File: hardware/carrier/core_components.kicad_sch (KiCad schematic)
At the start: 52 parts, among them J1 PANEL, J2 CARDKB, J3 HAPTIC, J4 EXT_LED, J5 PIEZ, J8 FRONTLIGHT, M1 Walter, Q1 UMH3N, Q2 SI1308EDL, Q3 MMST3904, SW1 KMR221GLFS, U1 CP2102N-A02-GQFN24, U2 SN74LVC2G126DCUR, U3 DRV2605LDGSR, U4 LIS2DW12TR

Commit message: Carrier: close the outline, tidy silkscreen, add GND pours (DRC 278 -> 28)
- Edge.Cuts rebuilt as a single closed loop (right edge 113.15, SIM notch, 1 mm corners)
- 0402/LGA parts moved to pager-carrier:*_NoSilk footprints (library copies without the
  silk outline), schematic fields updated; J6 silk box stops short of the shield pads;
  reference text re-placed or hidden; stale board texts removed
- GND pours both layers (0.2 clearance, thermal reliefs), 3 stitching vias for the
  top-side GND groups that had no path to the plane; all GND connected
- Remaining: 4 owner routing clearances, H1-H3 parked off-board, 2 unrouted nets

Co-Authored-By: Claude Fable 5.1 <noreply@anthropic.com>
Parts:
- C10, C11, C12, C2, C3, C4, C5, C9: footprint Capacitor_SMD:C_0402_1005Metric -> pager-carrier:C_0402_1005Metric_NoSilk
- R1, R10, R11, R14, R15, R16, R17, R18, R19, R2, R20, R21, R22, R3, R39, R4, R5, R6, R7, R8, R9: footprint Resistor_SMD:R_0402_1005Metric -> pager-carrier:R_0402_1005Metric_NoSilk
- U4: footprint Package_LGA:LGA-12_2x2mm_P0.5mm -> pager-carrier:LGA-12_2x2mm_P0.5mm_NoSilk
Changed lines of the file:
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@@
 			)
 		)
-		(property "Footprint" "Resistor_SMD:R_0402_1005Metric"
+		(property "Footprint" "pager-carrier:R_0402_1005Metric_NoSilk"
 			(at 196.85 39.37 0)
 			(hide yes)
@@
 			)
 		)
-		(property "Footprint" "Resistor_SMD:R_0402_1005Metric"
+		(property "Footprint" "pager-carrier:R_0402_1005Metric_NoSilk"
 			(at 199.39 101.6 0)
 			(hide yes)
@@
 			)
 		)
-		(property "Footprint" "Capacitor_SMD:C_0402_1005Metric"
+		(property "Footprint" "pager-carrier:C_0402_1005Metric_NoSilk"
 			(at 222.25 217.17 0)
 			(hide yes)
@@
 			)
 		)
-		(property "Footprint" "Resistor_SMD:R_0402_1005Metric"
+		(property "Footprint" "pager-carrier:R_0402_1005Metric_NoSilk"
 			(at 44.45 196.85 0)
 			(hide yes)
@@
 			)
 		)
-		(property "Footprint" "Resistor_SMD:R_0402_1005Metric"
+		(property "Footprint" "pager-carrier:R_0402_1005Metric_NoSilk"
 			(at 274.32 173.99 0)
 			(hide yes)
@@
 			)
 		)
-		(property "Footprint" "Package_LGA:LGA-12_2x2mm_P0.5mm"
+		(property "Footprint" "pager-carrier:LGA-12_2x2mm_P0.5mm_NoSilk"
 			(at 387.35 63.5 0)
 			(hide yes)
@@
 			)
 		)
-		(property "Footprint" "Resistor_SMD:R_0402_1005Metric"
+		(property "Footprint" "pager-carrier:R_0402_1005Metric_NoSilk"
 			(at 288.29 48.26 0)
 			(hide yes)
@@
 			)
 		)
-		(property "Footprint" "Resistor_SMD:R_0402_1005Metric"
+		(property "Footprint" "pager-carrier:R_0402_1005Metric_NoSilk"
 			(at 384.81 173.99 0)
 			(hide yes)
@@
 			)
 		)
-		(property "Footprint" "Capacitor_SMD:C_0402_1005Metric"
+		(property "Footprint" "pager-carrier:C_0402_1005Metric_NoSilk"
 			(at 318.77 176.53 0)
 			(hide yes)
@@
 			)
 		)
-		(property "Footprint" "Capacitor_SMD:C_0402_1005Metric"
+		(property "Footprint" "pager-carrier:C_0402_1005Metric_NoSilk"
 			(at 110.49 110.49 0)
 			(hide yes)
@@
 			)
 		)
-		(property "Footprint" "Resistor_SMD:R_0402_1005Metric"
+		(property "Footprint" "pager-carrier:R_0402_1005Metric_NoSilk"
 			(at 186.69 247.65 0)
 			(hide yes)
@@
 			)
 		)
-		(property "Footprint" "Resistor_SMD:R_0402_1005Metric"
+		(property "Footprint" "pager-carrier:R_0402_1005Metric_NoSilk"
 			(at 345.44 40.64 0)
 			(hide yes)
@@
 			)
 		)
-		(property "Footprint" "Resistor_SMD:R_0402_1005Metric"
+		(property "Footprint" "pager-carrier:R_0402_1005Metric_NoSilk"
 			(at 387.35 147.32 0)
 			(hide yes)
@@
 			)
 		)
-		(property "Footprint" "Capacitor_SMD:C_0402_1005Metric"
+		(property "Footprint" "pager-carrier:C_0402_1005Metric_NoSilk"
 			(at 33.02 233.68 0)
 			(hide yes)
@@
 			)
 		)
-		(property "Footprint" "Capacitor_SMD:C_0402_1005Metric"
+		(property "Footprint" "pager-carrier:C_0402_1005Metric_NoSilk"
 			(at 304.8 168.91 0)
 			(hide yes)
@@
 			)
 		)
-		(property "Footprint" "Resistor_SMD:R_0402_1005Metric"
+		(property "Footprint" "pager-carrier:R_0402_1005Metric_NoSilk"
 			(at 384.81 191.77 0)
 			(hide yes)
@@
 			)
 		)
-		(property "Footprint" "Resistor_SMD:R_0402_1005Metric"
+		(property "Footprint" "pager-carrier:R_0402_1005Metric_NoSilk"
 			(at 170.18 218.44 0)
 			(hide yes)
@@
 			)
 		)
-		(property "Footprint" "Resistor_SMD:R_0402_1005Metric"
+		(property "Footprint" "pager-carrier:R_0402_1005Metric_NoSilk"
 			(at 44.45 212.09 0)
 			(hide yes)
@@
 			)
 		)
-		(property "Footprint" "Resistor_SMD:R_0402_1005Metric"
+		(property "Footprint" "pager-carrier:R_0402_1005Metric_NoSilk"
 			(at 199.39 113.03 0)
 			(hide yes)
@@
 			)
 		)
-		(property "Footprint" "Resistor_SMD:R_0402_1005Metric"
+		(property "Footprint" "pager-carrier:R_0402_1005Metric_NoSilk"
 			(at 402.59 180.34 0)
 			(hide yes)
@@
 			)
 		)
-		(property "Footprint" "Resistor_SMD:R_0402_1005Metric"
+		(property "Footprint" "pager-carrier:R_0402_1005Metric_NoSilk"
 			(at 345.44 44.45 0)
 			(hide yes)
@@
 			)
 		)
-		(property "Footprint" "Resistor_SMD:R_0402_1005Metric"
+		(property "Footprint" "pager-carrier:R_0402_1005Metric_NoSilk"
 			(at 123.19 100.33 0)
 			(hide yes)
@@
 			)
 		)
-		(property "Footprint" "Capacitor_SMD:C_0402_1005Metric"
+		(property "Footprint" "pager-carrier:C_0402_1005Metric_NoSilk"
 			(at 101.6 213.36 0)
 			(hide yes)
@@
 			)
 		)
-		(property "Footprint" "Capacitor_SMD:C_0402_1005Metric"
+		(property "Footprint" "pager-carrier:C_0402_1005Metric_NoSilk"
 			(at 109.22 213.36 0)
 			(hide yes)
@@
 			)
 		)
-		(property "Footprint" "Resistor_SMD:R_0402_1005Metric"
+		(property "Footprint" "pager-carrier:R_0402_1005Metric_NoSilk"
 			(at 124.46 229.87 0)
 			(hide yes)
@@
 			)
 		)
-		(property "Footprint" "Resistor_SMD:R_0402_1005Metric"
+		(property "Footprint" "pager-carrier:R_0402_1005Metric_NoSilk"
 			(at 54.61 189.23 0)
 			(hide yes)
@@
 			)
 		)
-		(property "Footprint" "Resistor_SMD:R_0402_1005Metric"
+		(property "Footprint" "pager-carrier:R_0402_1005Metric_NoSilk"
 			(at 288.29 53.34 0)
 			(hide yes)
@@
 			)
 		)
-		(property "Footprint" "Resistor_SMD:R_0402_1005Metric"
+		(property "Footprint" "pager-carrier:R_0402_1005Metric_NoSilk"
 			(at 120.65 229.87 0)
 			(hide yes)
@@
 			)
 		)
-		(property "Footprint" "Resistor_SMD:R_0402_1005Metric"
+		(property "Footprint" "pager-carrier:R_0402_1005Metric_NoSilk"
 			(at 148.59 218.44 0)
 			(hide yes)
@@
 			)
 		)
-		(property "Footprint" "Capacitor_SMD:C_0402_1005Metric"
+		(property "Footprint" "pager-carrier:C_0402_1005Metric_NoSilk"
 			(at 334.01 66.04 0)
 			(hide yes)

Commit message: BOM: move six passives to JLC basic parts, fix connector LCSC codes (no footprint changes)
Carrier: R32 2.2M -> 1M (C26083), C14 22nF -> 100nF (C1525), R1 22.1k -> 22k (C25768),
R2 47.5k -> 47k (C25792); J1 LCSC C160407 (SM08B), J2 MPN/LCSC SM04B-SRSS-TB C160404
to match its SH footprint.
Panel: C11 4.7uF under basic code C19666, D1-D3 NSR0530 -> B5819W (C8598, SOD-123 as
already on the board), R4 2.2R gets C22939.
Board footprint fields updated to match. ERC clean on both.

Co-Authored-By: Claude Fable 5.1 <noreply@anthropic.com>
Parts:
- J1: LCSC C160409 -> C160407; MPN SM8B-SRSS-TB -> SM08B-SRSS-TB
- J2: LCSC C265102 -> C160404; MPN S4B-PH-SM4-TB -> SM04B-SRSS-TB
- R1: value 22.1k -> 22k; LCSC C43473 -> C25768; MPN 0402WGF2212TCE -> 0402WGF2202TCE
- R2: value 47.5k -> 47k; LCSC C25896 -> C25792; MPN 0402WGF4752TCE -> 0402WGF4702TCE
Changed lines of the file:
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@@
 			)
 		)
-		(property "MPN" "SM8B-SRSS-TB"
+		(property "MPN" "SM08B-SRSS-TB"
 			(at 181.61 69.85 0)
 			(hide yes)
@@
 			)
 		)
-		(property "LCSC" "C160409"
+		(property "LCSC" "C160407"
 			(at 181.61 72.39 0)
 			(hide yes)
@@
 			)
 		)
-		(property "Value" "22.1k"
+		(property "Value" "22k"
 			(at 36.322 196.85 0)
 			(show_name no)
@@
 			)
 		)
-		(property "MPN" "0402WGF2212TCE"
+		(property "MPN" "0402WGF2202TCE"
 			(at 43.18 210.82 0)
 			(hide yes)
@@
 			)
 		)
-		(property "LCSC" "C43473"
+		(property "LCSC" "C25768"
 			(at 43.18 213.36 0)
 			(hide yes)
@@
 			)
 		)
-		(property "MPN" "S4B-PH-SM4-TB"
+		(property "MPN" "SM04B-SRSS-TB"
 			(at 266.7 48.26 0)
 			(hide yes)
@@
 			)
 		)
-		(property "LCSC" "C265102"
+		(property "LCSC" "C160404"
 			(at 266.7 45.72 0)
 			(hide yes)
@@
 			)
 		)
-		(property "Value" "47.5k"
+		(property "Value" "47k"
 			(at 35.56 212.344 0)
 			(show_name no)
@@
 			)
 		)
-		(property "MPN" "0402WGF4752TCE"
+		(property "MPN" "0402WGF4702TCE"
 			(at 43.18 226.06 0)
 			(hide yes)
@@
 			)
 		)
-		(property "LCSC" "C25896"
+		(property "LCSC" "C25792"
 			(at 43.18 228.6 0)
 			(hide yes)

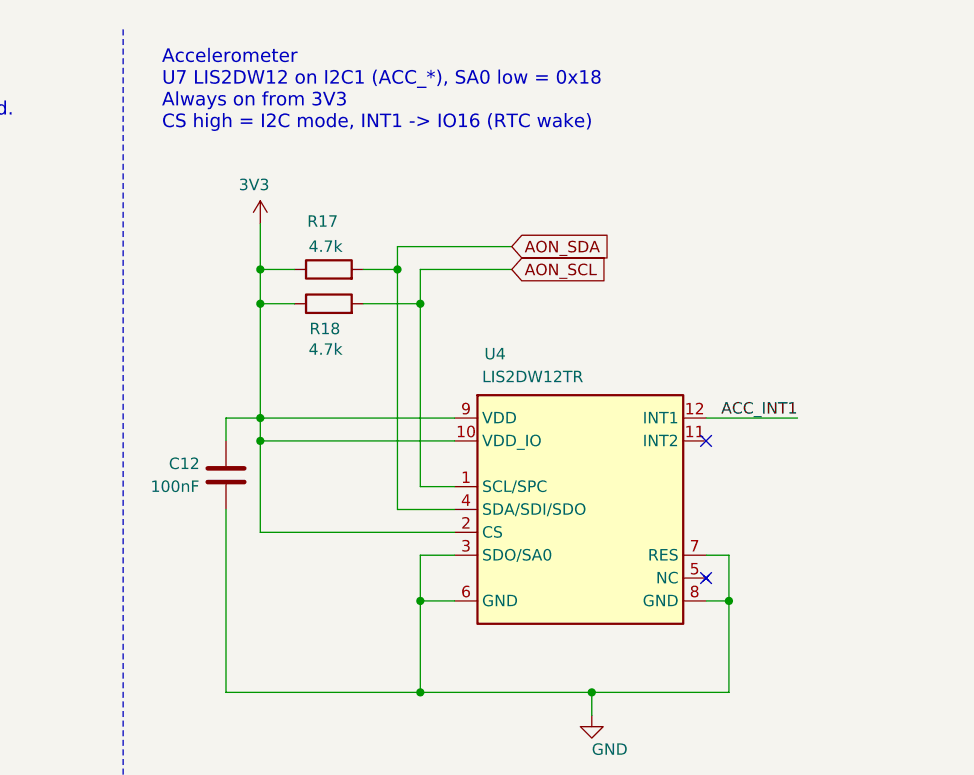
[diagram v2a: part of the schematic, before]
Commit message: Carrier: accelerometer -> MSKSEMI LIS2DW12TR-MS for Economic PCBA, JLC production files
U4 ST LIS2DW12TR (C189624, JLC "Standard Only") -> MSKSEMI LIS2DW12TR-MS
(C50385411, Economic and Standard). Same LGA-12 2x2 land pattern and pin-1
corner, different pinout (new project symbol); owner rerouted U4. The part is
an SC7A20-class die: WHO_AM_I 0x11, LIS3DH-style registers, I2C 0x18 with
SDO/SA0 low. Firmware follow-ups: accept 0x11, set SDO_PU in reg 0x57.

Also adds the ShouHan J6/SW2 footprints from the stock-part swap, the
Fabrication Toolkit options and production outputs (carrier and panel), and
the panel STEP. DRC 0 errors / 0 unconnected; ERC unchanged vs HEAD.

Co-Authored-By: Claude Opus 5.5 <noreply@anthropic.com>
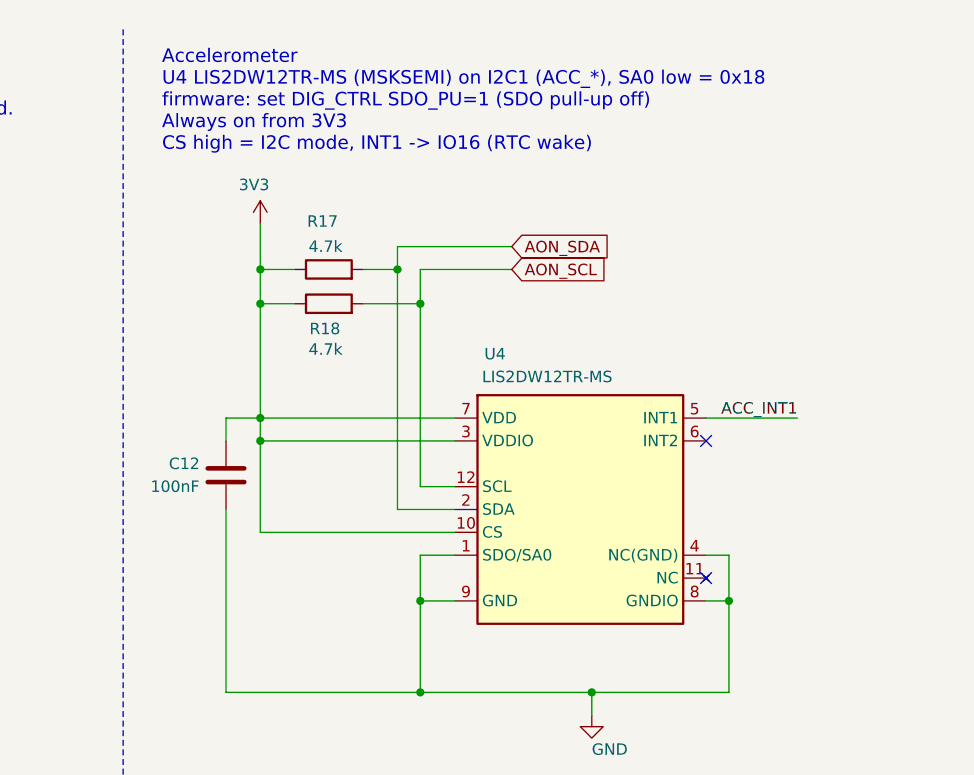
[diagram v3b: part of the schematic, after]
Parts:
- U4: value LIS2DW12TR -> LIS2DW12TR-MS; symbol pager-carrier:LIS2DW12TR -> pager-carrier:LIS2DW12TR-MS; LCSC C189624 -> C50385411; MPN LIS2DW12TR -> LIS2DW12TR-MS; Note (none) -> MSKSEMI SC7A20-class part, WHO_AM_I 0x11, LIS3DH-style regi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
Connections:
- net 3V3: now also U4.3 (VDDIO), U4.7 (VDD); no longer U4.2 (CS), U4.9 (VDD)
- net ACC_INT1: now also U4.5 (INT1); no longer U4.12 (INT1)
- net AON_SCL: now also U4.12 (SCL); no longer U4.1 (SCL/SPC)
- net AON_SDA: now also U4.2 (SDA); no longer U4.4 (SDA/SDI/SDO)
- net GND: now also U4.1 (SDO/SA0), U4.4 (NC(GND)), U4.9 (GND); no longer U4.3 (SDO/SA0), U4.6 (GND), U4.7 (RES)
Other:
- note added: "Accelerometer U4 LIS2DW12TR-MS (MSKSEMI) on I2C1 (ACC_*), SA0 low = 0x18 firmware: set DIG_CTRL SDO_PU=1 (SDO pull-up off) Always on from 3V3 CS high = I2C mode, INT1 -> IO16 (RTC wake)"
- note removed: "Accelerometer U7 LIS2DW12 on I2C1 (ACC_*), SA0 low = 0x18 Always on from 3V3 CS high = I2C mode, INT1 -> IO16 (RTC wake)"
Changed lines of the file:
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@@
 		)
 	)
-	(text "Accelerometer\nU7 LIS2DW12 on I2C1 (ACC_*), SA0 low = 0x18\nAlways on from 3V3\nCS high = I2C mode, INT1 -> IO16 (RTC wake)"
+	(text "Accelerometer\nU4 LIS2DW12TR-MS (MSKSEMI) on I2C1 (ACC_*), SA0 low = 0x18\nfirmware: set DIG_CTRL SDO_PU=1 (SDO pull-up off)\nAlways on from 3V3\nCS high = I2C mode, INT1 -> IO16 (RTC wake)"
 		(exclude_from_sim no)
 		(at 325.628 17.526 0)
@@
 	)
 	(symbol
-		(lib_id "pager-carrier:LIS2DW12TR")
+		(lib_id "pager-carrier:LIS2DW12TR-MS")
 		(at 372.11 68.58 0)
 		(unit 1)
@@
 			)
 		)
-		(property "Value" "LIS2DW12TR"
+		(property "Value" "LIS2DW12TR-MS"
 			(at 361.188 53.848 0)
 			(show_name no)
@@
 			)
 		)
-		(property "Datasheet" "https://www.st.com/resource/en/datasheet/lis2dw12.pdf"
+		(property "Datasheet" "https://www.lcsc.com/datasheet/C50385411.pdf"
 			(at 387.35 66.04 0)
 			(hide yes)
@@
 			)
 		)
-		(property "Description" "3-axis MEMS accelerometer, I2C/SPI, LGA-12 2x2 mm"
+		(property "Description" "3-axis accelerometer, I2C/SPI, LGA-12 2x2 mm (MSKSEMI, SC7A20-class)"
 			(at 387.35 68.58 0)
 			(hide yes)
@@
 			)
 		)
-		(property "MPN" "LIS2DW12TR"
+		(property "MPN" "LIS2DW12TR-MS"
 			(at 372.11 83.82 0)
 			(hide yes)
@@
 			)
 		)
-		(property "LCSC" "C189624"
+		(property "LCSC" "C50385411"
 			(at 372.11 86.36 0)
 			(hide yes)
@@
 			)
 		)
+		(property "Note" "MSKSEMI SC7A20-class part, WHO_AM_I 0x11, LIS3DH-style registers; swapped from ST LIS2DW12TR 25 Oct 2026 for Economic PCBA"
+			(at 372.11 91.44 0)
+			(hide yes)
+			(show_name no)
+			(do_not_autoplace no)
+			(effects
+				(font
+					(size 1.27 1.27)
+				)
+			)
+		)
 		(property "DNP" ""
 			(at 372.11 88.9 0)
@@
 			)
 		)
-		(pin "9"
+		(pin "7"
+		)
+		(pin "3"
+		)
+		(pin "12"
+		)
+		(pin "2"
 		)
 		(pin "10"
@@
 		(pin "1"
 		)
-		(pin "4"
-		)
-		(pin "2"
+		(pin "9"
 		)
-		(pin "3"
+		(pin "5"
 		)
 		(pin "6"
 		)
-		(pin "12"
+		(pin "4"
 		)
 		(pin "11"
 		)
-		(pin "7"
-		)
-		(pin "5"
-		)
 		(pin "8"
